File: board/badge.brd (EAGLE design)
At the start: 157.7 x 91.3 mm, 44 parts, among them IC1 STM32F030F4, IC2 UBLOX_MAX, IC3 RFM69HW, IC4 MCP1640, J2 20-0096, J3 SWD_PTH_SHROUD, X1 RADIOMETRIX-MTX2, X2 SMA-142-0701-851/861, X3 091OLED

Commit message: drc fixes
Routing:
- net 0V: track 318.4 -> 314.0 mm
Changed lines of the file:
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@@
 <layer number="49" name="Reference" color="7" fill="1" visible="no" active="yes"/>
 <layer number="50" name="dxf" color="7" fill="1" visible="no" active="no"/>
-<layer number="51" name="tDocu" color="14" fill="1" visible="no" active="yes"/>
-<layer number="52" name="bDocu" color="11" fill="1" visible="no" active="yes"/>
+<layer number="51" name="tDocu" color="14" fill="1" visible="yes" active="yes"/>
+<layer number="52" name="bDocu" color="11" fill="1" visible="yes" active="yes"/>
 <layer number="53" name="tGND_GNDA" color="7" fill="9" visible="no" active="no"/>
 <layer number="54" name="bGND_GNDA" color="1" fill="9" visible="no" active="no"/>
@@
 <wire x1="34" y1="53.15" x2="34.15" y2="53.15" width="0.6096" layer="16"/>
 <wire x1="34.15" y1="53.15" x2="35.25" y2="54.25" width="0.6096" layer="16"/>
-<wire x1="35.25" y1="54.25" x2="35.25" y2="55.25" width="0.6096" layer="16"/>
+<wire x1="35.25" y1="54.25" x2="35.25" y2="55" width="0.6096" layer="16"/>
 <wire x1="40" y1="27.524" x2="40" y2="29.78" width="0.254" layer="16"/>
 <wire x1="40" y1="29.78" x2="40.72" y2="30.5" width="0.254" layer="16"/>
@@
 <wire x1="20.75" y1="68.25" x2="21.1" y2="68.25" width="0.254" layer="16"/>
 <wire x1="21.35" y1="68" x2="21.75" y2="68" width="0.254" layer="16"/>
-<wire x1="21.75" y1="68" x2="22.5" y2="67.25" width="0.254" layer="16"/>
-<wire x1="22.5" y1="67.25" x2="22.5" y2="66.5" width="0.254" layer="16"/>
+<wire x1="21.75" y1="68" x2="22.5" y2="67" width="0.254" layer="16"/>
+<wire x1="22.5" y1="67" x2="22.5" y2="66.5" width="0.254" layer="16"/>
 <wire x1="22.5" y1="66.5" x2="22.75" y2="66.25" width="0.254" layer="16"/>
 <wire x1="22.75" y1="66.25" x2="24.25" y2="66.25" width="0.254" layer="16"/>
@@
 <wire x1="25" y1="65.5" x2="25" y2="64.5475" width="0.254" layer="16"/>
 <wire x1="25" y1="64.5475" x2="24.9525" y2="64.5" width="0.254" layer="16"/>
-<wire x1="35.25" y1="55.25" x2="36.5" y2="56.5" width="0.6096" layer="16"/>
-<wire x1="36.5" y1="56.5" x2="36.75" y2="56.5" width="0.6096" layer="16"/>
-<wire x1="36.75" y1="56.5" x2="37.5" y2="57.25" width="0.6096" layer="16"/>
+<wire x1="35.25" y1="55" x2="37.5" y2="57.25" width="0.6096" layer="16"/>
 <wire x1="37.5" y1="57.25" x2="37.5" y2="59.75" width="0.6096" layer="16"/>
 <wire x1="37.5" y1="59.75" x2="38" y2="60.25" width="0.6096" layer="16"/>
@@
 <wire x1="23.75" y1="28" x2="21" y2="28" width="0.4064" layer="1"/>
 <wire x1="21" y1="28" x2="20.5" y2="28.5" width="0.4064" layer="1"/>
-<wire x1="20.5" y1="28.5" x2="20.5" y2="32" width="0.4064" layer="1"/>
-<wire x1="20.5" y1="32" x2="22.5" y2="34" width="0.4064" layer="1"/>
+<wire x1="20.5" y1="28.5" x2="20.5" y2="31.75" width="0.4064" layer="1"/>
 <wire x1="22.5" y1="34" x2="31.75" y2="34" width="0.4064" layer="1"/>
 <wire x1="31.75" y1="34" x2="34" y2="31.75" width="0.4064" layer="1"/>
@@
 <wire x1="34.125" y1="26.5" x2="34.375" y2="26.75" width="0.4064" layer="1"/>
 <wire x1="34.375" y1="26.75" x2="34.5" y2="26.75" width="0.4064" layer="1"/>
-<wire x1="34.5" y1="26.75" x2="35.375" y2="27.125" width="0.4064" layer="1"/>
 <via x="18.5" y="28.5" extent="1-16" drill="0.381" shape="octagon"/>
 <wire x1="18.5" y1="28.5" x2="18.5" y2="33.5" width="0.254" layer="1"/>
@@
 <wire x1="34" y1="31.375" x2="35.625" y2="29.75" width="0.3048" layer="1"/>
 <wire x1="35.625" y1="29.75" x2="35.625" y2="27.375" width="0.3048" layer="1"/>
-<wire x1="35.625" y1="27.375" x2="35.375" y2="27.125" width="0.3048" layer="1"/>
 <wire x1="34.125" y1="22.625" x2="34.125" y2="22.25" width="0.3048" layer="1"/>
 <wire x1="34.125" y1="22.25" x2="34.5" y2="21.875" width="0.3048" layer="1"/>
@@
 <vertex x="34.25" y="31.25"/>
 <vertex x="32.375" y="33.875"/>
-<vertex x="22.625" y="33.875"/>
-<vertex x="20.875" y="31.875"/>
+<vertex x="22.375" y="34.125"/>
+<vertex x="20.625" y="32.125"/>
 <vertex x="20.625" y="29.5"/>
 <vertex x="21" y="29.125"/>
@@
 <via x="32.75" y="33.25" extent="1-16" drill="0.381" shape="octagon"/>
 <via x="34.25" y="31.75" extent="1-16" drill="0.381" shape="octagon"/>
-<via x="20.5" y="32" extent="1-16" drill="0.381" shape="octagon"/>
+<via x="20.5" y="31.75" extent="1-16" drill="0.381" shape="octagon"/>
 <via x="21.75" y="28.5" extent="1-16" drill="0.381" shape="octagon"/>
 <via x="34.5" y="25.5" extent="1-16" drill="0.381" shape="octagon"/>
@@
 <via x="28.25" y="37.25" extent="1-16" drill="0.381" shape="octagon"/>
 <via x="46.5" y="53.5" extent="1-16" drill="0.381" shape="octagon"/>
-<via x="33.75" y="74" extent="1-16" drill="0.381" shape="octagon"/>
+<via x="32.75" y="74.5" extent="1-16" drill="0.381" shape="octagon"/>
 <via x="37.5" y="73.25" extent="1-16" drill="0.381" shape="octagon"/>
 <wire x1="25.5" y1="68.95" x2="25.2" y2="68.95" width="0.4064" layer="16"/>
@@
 <vertex x="21.75" y="45.25"/>
 <vertex x="28.25" y="39.25"/>
-<vertex x="24.75" y="35.75"/>
-<vertex x="17.75" y="28.25"/>
+<vertex x="24.75" y="36.25"/>
+<vertex x="17.75" y="28.75"/>
 <vertex x="16.25" y="29.75"/>
 <vertex x="18.25" y="32.25"/>
@@
 <wire x1="21.4" y1="69.25" x2="21.35" y2="68.95" width="0.254" layer="16"/>
 <wire x1="25.5" y1="67.05" x2="23.65" y2="67.05" width="0.8128" layer="16"/>
-<wire x1="22.25" y1="69" x2="22.25" y2="68.2" width="0.254" layer="16"/>
+<wire x1="22.25" y1="69" x2="22.25" y2="68.45" width="0.254" layer="16"/>
 <wire x1="25.5" y1="67.05" x2="32.576096875" y2="67.05" width="0.8128" layer="16"/>
 <wire x1="32.576096875" y1="67.05" x2="32.626096875" y2="67" width="0.254" layer="16"/>
@@
 <wire x1="20.75" y1="73.25" x2="20.25" y2="73.25" width="0.8128" layer="16"/>
 <wire x1="20.25" y1="73.25" x2="20" y2="73" width="0.8128" layer="16"/>
-<wire x1="22.25" y1="68.2" x2="22.3" y2="68.2" width="0.254" layer="16"/>
-<wire x1="22.3" y1="68.2" x2="23" y2="67.5" width="0.254" layer="16"/>
-<wire x1="23" y1="67.5" x2="23" y2="67.25" width="0.254" layer="16"/>
-<wire x1="23" y1="67.25" x2="23.25" y2="67" width="0.254" layer="16"/>
+<wire x1="22.25" y1="68.45" x2="22.3" y2="68.2" width="0.254" layer="16"/>
+<wire x1="22.3" y1="68.2" x2="23.25" y2="67" width="0.254" layer="16"/>
 <wire x1="23.25" y1="67" x2="23.6" y2="67" width="0.254" layer="16"/>
 <wire x1="23.6" y1="67" x2="23.65" y2="67.05" width="0.254" layer="16"/>

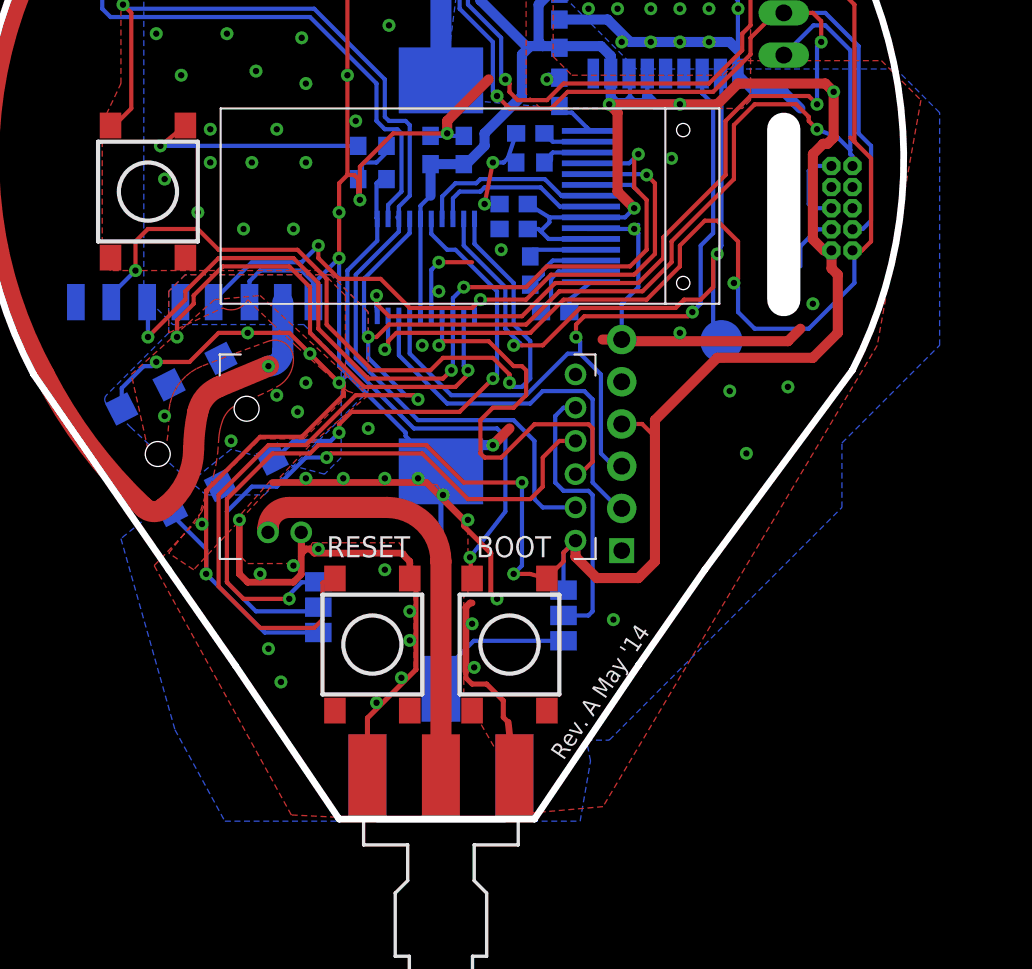
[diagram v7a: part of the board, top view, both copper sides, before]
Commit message: adding part numbers
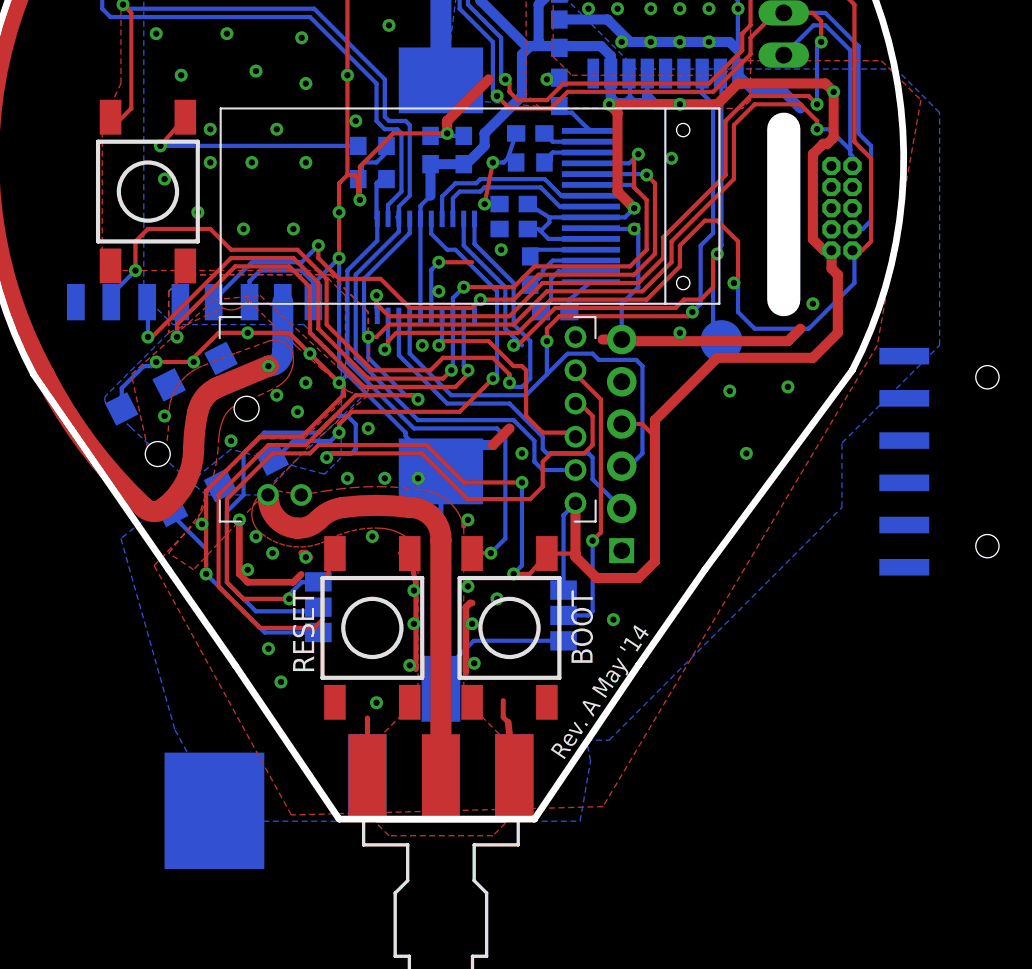
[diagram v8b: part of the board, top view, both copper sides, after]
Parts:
- added JP2: (no value), SparkFun-Connectors:1X06-SMD
- C10, C3, C5: value (none) -> 100n
- C11: value (none) -> 4u7
- C12: value (none) -> 10u
- C6, C9: value (none) -> 1u
- L1: value INDUCTOR -> 4u7
- R1: value (none) -> 10k
- R2: value (none) -> 390k
- R4: value (none) -> 976k
- R5: value (none) -> 562k
- R6, R7: value (none) -> 330
- S1, S2, S3: value SWITCH-MOMENTARY-2 -> SWITCH-MOMENTARY-2W; device SparkFun-Electromechanical:TACTILE_SWITCH_TALL -> ukhas:TACTILE_WIDE
- moved X1 2.25 mm to (30.8, 38.0)
- moved S2 1.00 mm to (28.5, 25.2)
- moved S3 1.00 mm to (36.8, 25.2)
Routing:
- net 0V: track 314.0 -> 271.5 mm, vias 114 -> 115
- net N$18: track 36.6 -> 48.4 mm
- net TX: track 25.9 -> 14.2 mm
- net N$8: track 47.0 -> 52.5 mm
- net +3V3: track 208.8 -> 212.5 mm
- net N$9: track 23.1 -> 20.8 mm
- net TX_EN: track 64.1 -> 61.9 mm
- net N$4: track 26.7 -> 27.9 mm
- net N$7: track 32.8 -> 32.1 mm
- net N$20: track 16.8 -> 17.2 mm, vias 0 -> 1
- added copper zone on layer 1, net N$21
